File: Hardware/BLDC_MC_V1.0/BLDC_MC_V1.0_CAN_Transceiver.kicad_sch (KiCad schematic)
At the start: 15 parts, among them U2 TCAN334DR

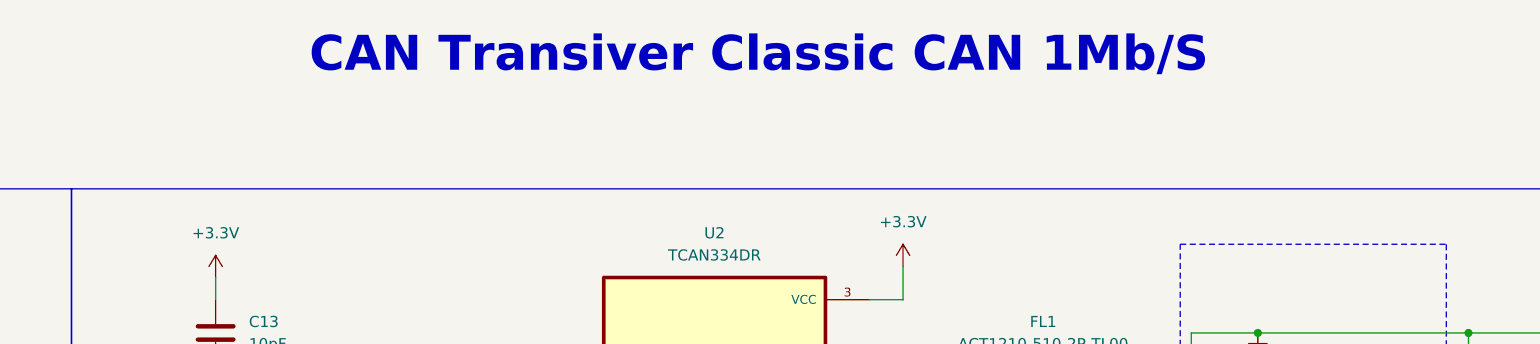
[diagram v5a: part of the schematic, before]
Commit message: Adjust the connections between sheets
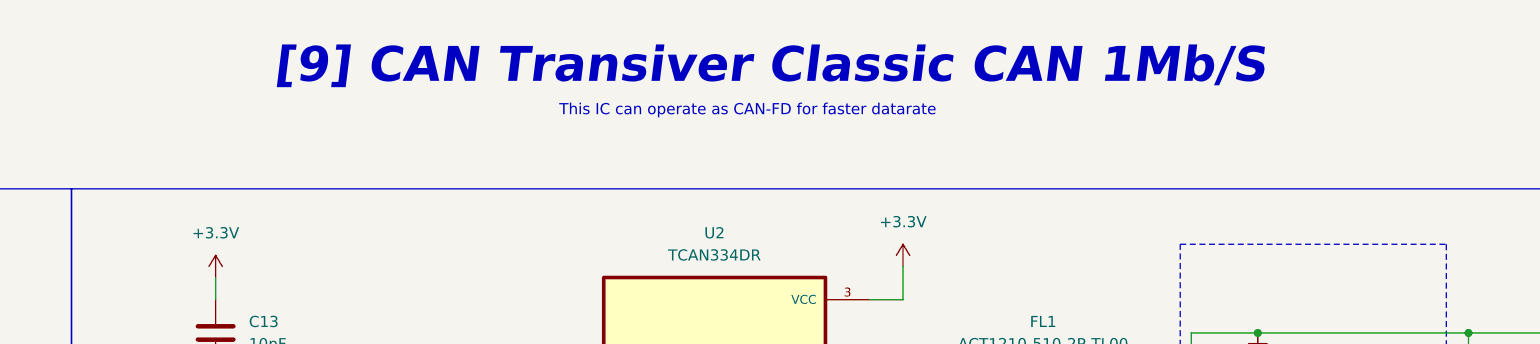
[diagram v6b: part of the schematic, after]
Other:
- note added: "This IC can operate as CAN-FD for faster datarate"
- note added: "[9] CAN Transiver Classic CAN 1Mb/S"
- note removed: "CAN Transiver Classic CAN 1Mb/S"
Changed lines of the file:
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@@
 		)
 	)
-	(text "CAN Transiver Classic CAN 1Mb/S"
+	(text "[9] CAN Transiver Classic CAN 1Mb/S"
 		(exclude_from_sim no)
-		(at 143.51 46.99 0)
+		(at 144.78 48.26 0)
 		(effects
 			(font
@@
 				(thickness 0.8)
 				(bold yes)
+				(italic yes)
 				(color 132 0 0 1)
 			)
@@
 			)
 		)
+	)
+	(text "This IC can operate as CAN-FD for faster datarate\n"
+		(exclude_from_sim no)
+		(at 142.24 53.34 0)
+		(effects
+			(font
+				(size 1.27 1.27)
+			)
+		)

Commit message: Solve all errors and wornings in project
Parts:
- CR1: Assembled (none) -> Yes; LCSC_PN (none) -> C6251381; MP (none) -> PESD2CANFD24V-QCZ
